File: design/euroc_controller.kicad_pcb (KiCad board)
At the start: 4 copper layers, 35.1 x 75.7 mm, 82 parts, among them J1 xt30, J2 jst_sh 4, J4 jst_sh 4, J5 jst_sh 4, J6 SMA, J7 Screw_Terminal_01x06, J8 USB_C_Receptacle_USB2.0, J9 jst_sh 4, Q1 MMBT3904, U1 TPSM5601R5, U10 VN7050ASTR, U11 VN7050ASTR, U12 STM32L562CETx, U2 USBLC6-2SC6, U3 LSM6DSO32, U4 MS5611-01BA, U5 SN65HVD232, U6 W25Q128JVS, U7 RFM69W, U8 L86, U9 VN7050ASTR, Y1 48MHz

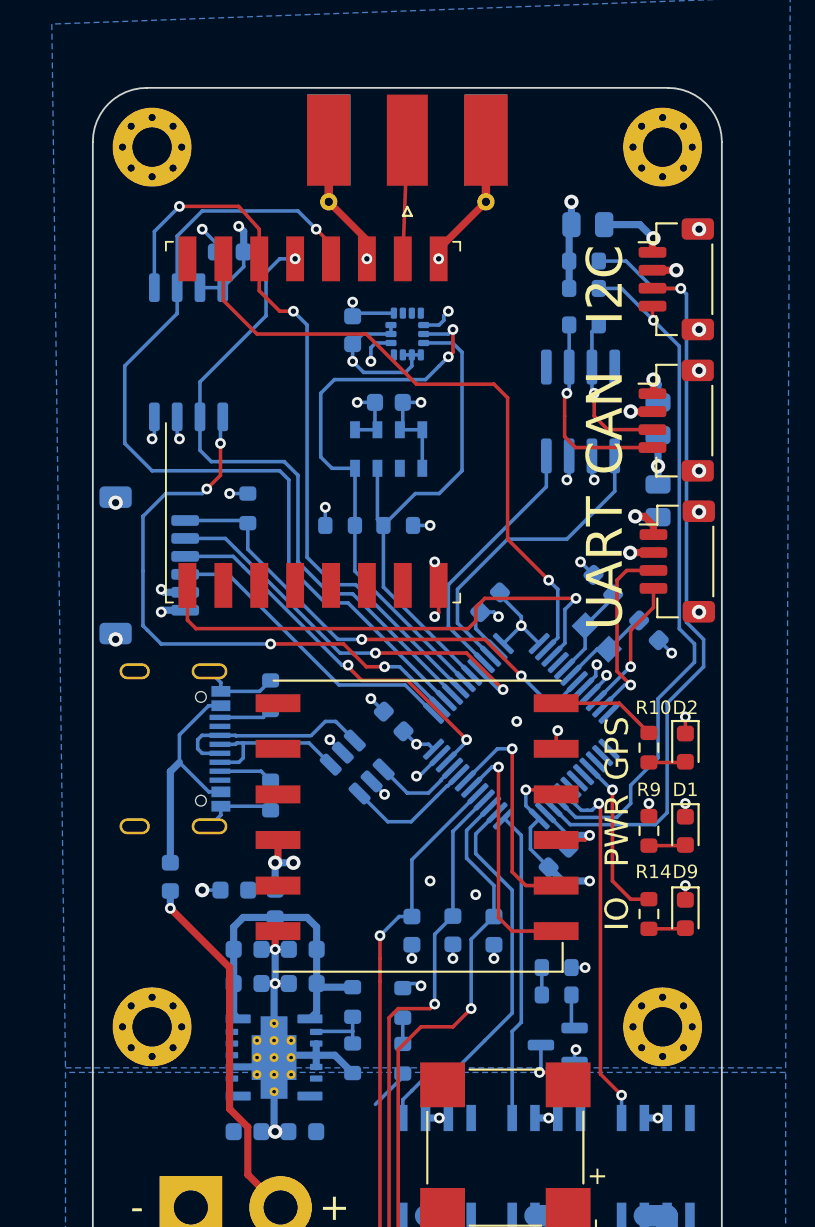
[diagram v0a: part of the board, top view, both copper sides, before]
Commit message: align mounting holes
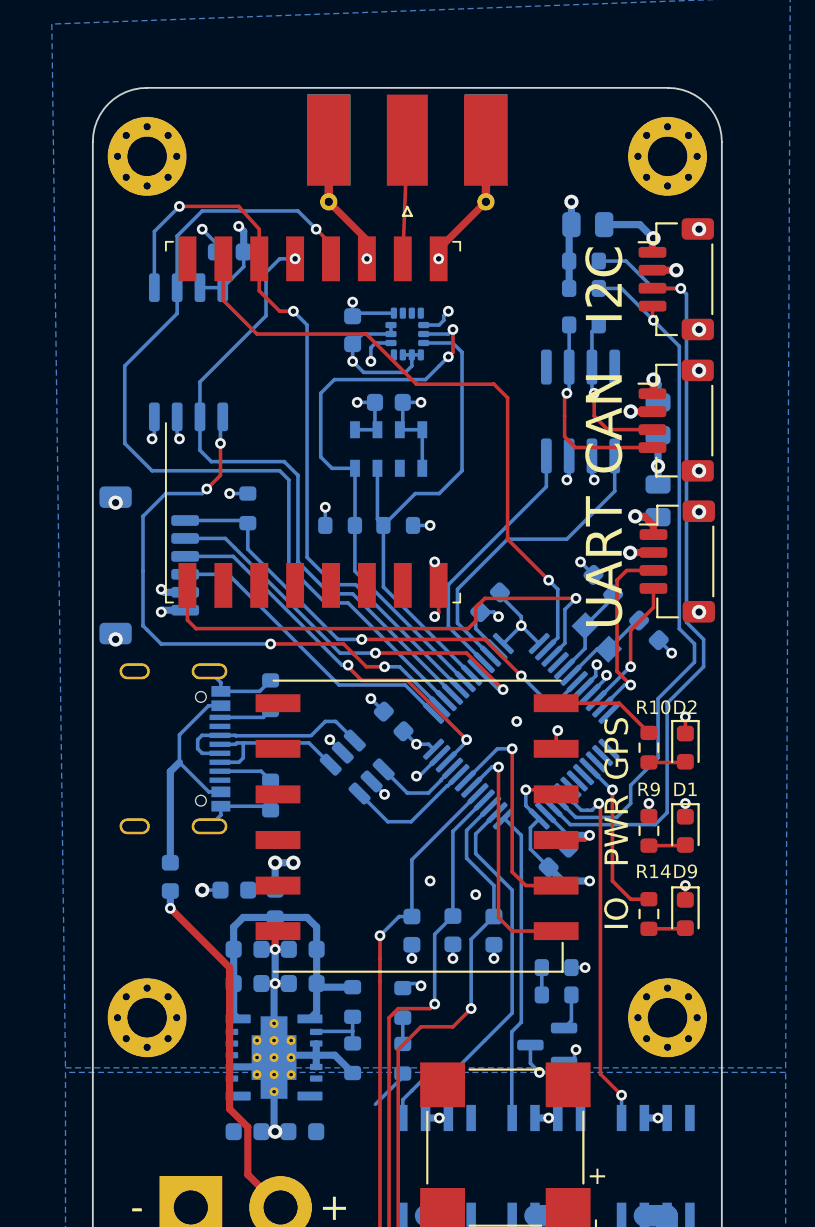
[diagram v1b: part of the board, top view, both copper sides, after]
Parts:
- removed the H1 at (196.1, 49.0)
- removed the H2 at (167.6, 49.0)
- added H3: MountingHole_Pad, MountingHole:MountingHole_2.2mm_M2_Pad_Via, F.Cu at (167.4, 97.5)
- added H4: MountingHole_Pad, MountingHole:MountingHole_2.2mm_M2_Pad_Via, F.Cu at (196.4, 97.5)
- moved H1 48.5 mm to (167.4, 49.5)
- moved H2 48.5 mm to (196.4, 49.5)
- moved Q1 0.59 mm to (189.7, 99.1)
- renumbered H3 to H1, H4 to H2
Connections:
- U8 pad 10: +3V3 -> unconnected-(U8-~{RESET}-Pad10)
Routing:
- net +3V3: track 64.1 -> 62.8 mm
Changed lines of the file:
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@@
   (net 95 "Net-(J5-Pin_1)")
   (net 96 "Net-(J4-Pin_1)")
+  (net 97 "unconnected-(U8-~{RESET}-Pad10)")
   (footprint "Connector_JST:JST_SH_BM04B-SRSS-TB_1x04-1MP_P1.00mm_Vertical" (layer "F.Cu")
     (at 196.846934 64.262 -90)
@@
       (net 42 "unconnected-(U8-NC-Pad9)") (pinfunction "NC") (pintype "no_connect"))
     (pad "10" smd rect (at 7.75 -0.77) (size 2.5 1) (layers "F.Cu" "F.Paste" "F.Mask")
-      (net 3 "+3V3") (pinfunction "~{RESET}") (pintype "input"))
+      (net 97 "unconnected-(U8-~{RESET}-Pad10)") (pinfunction "~{RESET}") (pintype "input+no_connect"))
     (pad "11" smd rect (at 7.75 -3.31) (size 2.5 1) (layers "F.Cu" "F.Paste" "F.Mask")
       (net 43 "unconnected-(U8-RESERVED-Pad11)") (pinfunction "RESERVED") (pintype "passive+no_connect"))
@@
   )
   (footprint "MountingHole:MountingHole_2.2mm_M2_Pad_Via" (layer "F.Cu")
-    (at 196.088 49.022)
+    (at 167.364 97.536)
     (descr "Mounting Hole 2.2mm, M2")
     (tags "mounting hole 2.2mm m2")
@@
     (property "ki_keywords" "mounting hole")
     (attr exclude_from_pos_files)
-    (fp_text reference "H1" (at 0 -3.2) (layer "F.SilkS") hide
+    (fp_text reference "H3" (at 0 -3.2) (layer "F.SilkS") hide
         (effects (font (size 1 1) (thickness 0.15)))
     )
@@
   )
   (footprint "MountingHole:MountingHole_2.2mm_M2_Pad_Via" (layer "F.Cu")
-    (at 167.64 49.022)
+    (at 196.364 97.536)
     (descr "Mounting Hole 2.2mm, M2")
     (tags "mounting hole 2.2mm m2")
@@
     (property "ki_keywords" "mounting hole")
     (attr exclude_from_pos_files)
-    (fp_text reference "H2" (at 0 -3.2) (layer "F.SilkS") hide
+    (fp_text reference "H4" (at 0 -3.2) (layer "F.SilkS") hide
         (effects (font (size 1 1) (thickness 0.15)))
     )
@@
   )
   (footprint "MountingHole:MountingHole_2.2mm_M2_Pad_Via" (layer "F.Cu")
-    (at 196.088 98.044)
+    (at 196.364 49.536)
     (descr "Mounting Hole 2.2mm, M2")
     (tags "mounting hole 2.2mm m2")
@@
     (property "ki_keywords" "mounting hole")
     (attr exclude_from_pos_files)
-    (fp_text reference "H4" (at 0 -3.2) (layer "F.SilkS") hide
+    (fp_text reference "H2" (at 0 -3.2) (layer "F.SilkS") hide
         (effects (font (size 1 1) (thickness 0.15)))
     )
@@
   )
   (footprint "MountingHole:MountingHole_2.2mm_M2_Pad_Via" (layer "F.Cu")
-    (at 167.64 98.044)
+    (at 167.364 49.536)
     (descr "Mounting Hole 2.2mm, M2")
     (tags "mounting hole 2.2mm m2")
@@
     (property "ki_keywords" "mounting hole")
     (attr exclude_from_pos_files)
-    (fp_text reference "H3" (at 0 -3.2) (layer "F.SilkS") hide
+    (fp_text reference "H1" (at 0 -3.2) (layer "F.SilkS") hide
         (effects (font (size 1 1) (thickness 0.15)))
     )
@@
   )
   (footprint "Package_TO_SOT_SMD:SOT-23" (layer "B.Cu")
-    (at 190.246 99.06 180)
+    (at 189.6595 99.06 180)
     (descr "SOT, 3 Pin (https://www.jedec.org/system/files/docs/to-236h.pdf variant AB), generated with kicad-footprint-generator ipc_gullwing_generator.py")
     (tags "SOT TO_SOT_SMD")
@@
     (property "ki_keywords" "NPN Transistor")
     (attr smd)
-    (fp_text reference "Q1" (at 1.778 1.27) (layer "B.SilkS")
+    (fp_text reference "Q1" (at 1.9535 1.27) (layer "B.SilkS")
         (effects (font (size 1 1) (thickness 0.15)) (justify mirror))
     )
@@
   (segment (start 174.437 95.692) (end 174.498 95.631) (width 0.4) (layer "B.Cu") (net 1))
   (segment (start 190.834016 87.376004) (end 189.566342 86.10833) (width 0.2) (layer "B.Cu") (net 1))
-  (segment (start 191.1835 100.01) (end 191.1835 99.3925) (width 0.2) (layer "B.Cu") (net 1))
   (segment (start 191.389 116.002) (end 190.551 116.84) (width 0.8) (layer "B.Cu") (net 1))
   (segment (start 165.608 68.82) (end 165.608 68.834) (width 0.4) (layer "B.Cu") (net 1))
@@
   (segment (start 191.389 114.808) (end 191.389 116.002) (width 0.8) (layer "B.Cu") (net 1))
   (segment (start 191.1835 99.3925) (end 191.262 99.314) (width 0.2) (layer "B.Cu") (net 1))
+  (segment (start 191.1835 99.822) (end 191.1835 99.3925) (width 0.2) (layer "B.Cu") (net 1))
   (segment (start 184.404 93.4465) (end 184.404 94.234) (width 0.2) (layer "B.Cu") (net 1))
   (segment (start 186.69 74.93) (end 186.944 75.184) (width 0.2) (layer "B.Cu") (net 1))
@@
   (segment (start 179.874334 84.370334) (end 180.594 85.09) (width 0.2) (layer "B.Cu") (net 1))
   (segment (start 182.532028 84.074) (end 182.372 84.074) (width 0.2) (layer "B.Cu") (net 1))
+  (segment (start 190.9955 100.01) (end 191.1835 99.822) (width 0.2) (layer "B.Cu") (net 1))
   (segment (start 171.471 86.239) (end 170.84 86.87) (width 0.2) (layer "B.Cu") (net 1))
   (segment (start 169.48151 73.82764) (end 168.31564 73.82764) (width 0.4) (layer "B.Cu") (net 1))
@@
   (segment (start 195.874008 76.494008) (end 196.596 77.216) (width 0.2) (layer "B.Cu") (net 1))
   (segment (start 165.608 76.42) (end 165.608 76.454) (width 0.4) (layer "B.Cu") (net 1))
+  (segment (start 190.597 100.01) (end 190.9955 100.01) (width 0.2) (layer "B.Cu") (net 1))
   (segment (start 182.114 61.218) (end 181.756 61.576) (width 0.2) (layer "B.Cu") (net 1))
   (segment (start 173.634 79.35) (end 174.244 78.74) (width 0.2) (layer "B.Cu") (net 1))
@@
   (segment (start 189.903945 84.836) (end 190.157945 85.09) (width 0.2) (layer "F.Cu") (net 3))
   (segment (start 191.77 110.744) (end 192.532 110.744) (width 0.4) (layer "F.Cu") (net 3))
-  (segment (start 174.657945 88.740055) (end 174.498 88.9) (width 0.4) (layer "F.Cu") (net 3))
   (segment (start 183.61 72.358) (end 183.388 72.136) (width 0.2) (layer "F.Cu") (net 3))
   (segment (start 183.61 73.445) (end 183.61 74.962) (width 0.2) (layer "F.Cu") (net 3))
   (segment (start 183.61 73.445) (end 183.61 72.358) (width 0.2) (layer "F.Cu") (net 3))
-  (segment (start 174.657945 87.63) (end 174.657945 88.740055) (width 0.4) (layer "F.Cu") (net 3))
   (segment (start 190.825 109.799) (end 191.77 110.744) (width 0.4) (layer "F.Cu") (net 3))
   (segment (start 195.326 86.297) (end 195.326 85.598) (width 0.2) (layer "F.Cu") (net 3))
@@
   (segment (start 190.134 100.584) (end 190.825 101.275) (width 0.2) (layer "F.Cu") (net 4))
   (via (at 189.23 100.584) (size 0.6) (drill 0.3) (layers "F.Cu" "B.Cu") (net 4))
-  (segment (start 189.3085 99.06) (end 189.3085 100.5055) (width 0.2) (layer "B.Cu") (net 4))
-  (segment (start 189.3085 100.5055) (end 189.23 100.584) (width 0.2) (layer "B.Cu") (net 4))
+  (segment (start 188.722 99.06) (end 188.722 100.076) (width 0.2) (layer "B.Cu") (net 4))
+  (segment (start 188.722 100.076) (end 189.23 100.584) (width 0.2) (layer "B.Cu") (net 4))
   (segment (start 197.3205 87.947) (end 197.358 87.9095) (width 0.2) (layer "F.Cu") (net 5))
   (segment (start 195.326 87.947) (end 197.3205 87.947) (width 0.2) (layer "F.Cu") (net 5))
@@
   (segment (start 192.154 85.976) (end 192.532 85.598) (width 0.2) (layer "B.Cu") (net 82))
   (segment (start 191.894 85.976) (end 192.154 85.976) (width 0.2) (layer "B.Cu") (net 82))
+  (segment (start 187.706 103.124) (end 187.6845 103.1025) (width 0.2) (layer "B.Cu") (net 83))
   (segment (start 187.299884 86.461884) (end 188.214 87.376) (width 0.2) (layer "B.Cu") (net 83))
-  (segment (start 187.706 98.298) (end 187.706 103.124) (width 0.2) (layer "B.Cu") (net 83))
-  (segment (start 188.214 97.79) (end 187.706 98.298) (width 0.2) (layer "B.Cu") (net 83))
+  (segment (start 187.6845 98.3195) (end 188.214 97.79) (width 0.2) (layer "B.Cu") (net 83))
   (segment (start 187.215212 86.461884) (end 187.299884 86.461884) (width 0.2) (layer "B.Cu") (net 83))
+  (segment (start 187.6845 103.1025) (end 187.6845 98.3195) (width 0.2) (layer "B.Cu") (net 83))
   (segment (start 188.214 87.376) (end 188.214 97.79) (width 0.2) (layer "B.Cu") (net 83))
   (segment (start 181.61 103.124) (end 181.61 102.108) (width 0.2) (layer "B.Cu") (net 84))
@@
   (segment (start 186.948652 79.248) (end 187.198 79.248) (width 0.2) (layer "B.Cu") (net 90))
   (segment (start 185.800998 78.100346) (end 186.948652 79.248) (width 0.2) (layer "B.Cu") (net 90))
+  (segment (start 191.008 97.699) (end 190.597 98.11) (width 0.2) (layer "B.Cu") (net 91))
   (segment (start 191.008 97.9345) (end 191.1835 98.11) (width 0.2) (layer "B.Cu") (net 91))
-  (segment (start 191.008 96.266) (end 191.008 97.9345) (width 0.2) (layer "B.Cu") (net 91))
+  (segment (start 191.008 96.266) (end 191.008 97.699) (width 0.2) (layer "B.Cu") (net 91))
   (segment (start 170.434 82.804) (end 170.438 82.8) (width 0.2) (layer "B.Cu") (net 92))
   (segment (start 171.42 81.8) (end 172.290001 81.8) (width 0.2) (layer "B.Cu") (net 92))

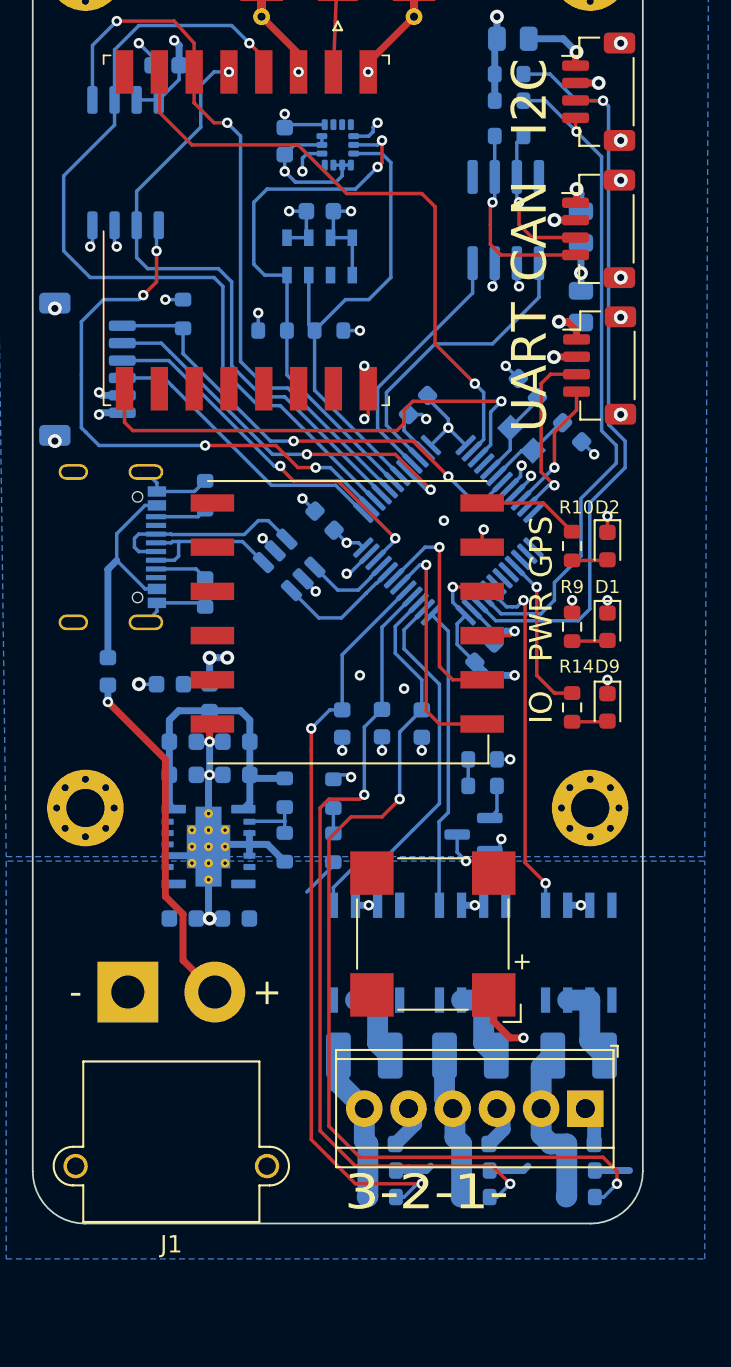
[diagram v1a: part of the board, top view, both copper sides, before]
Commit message: use real clock, fix esd vbus
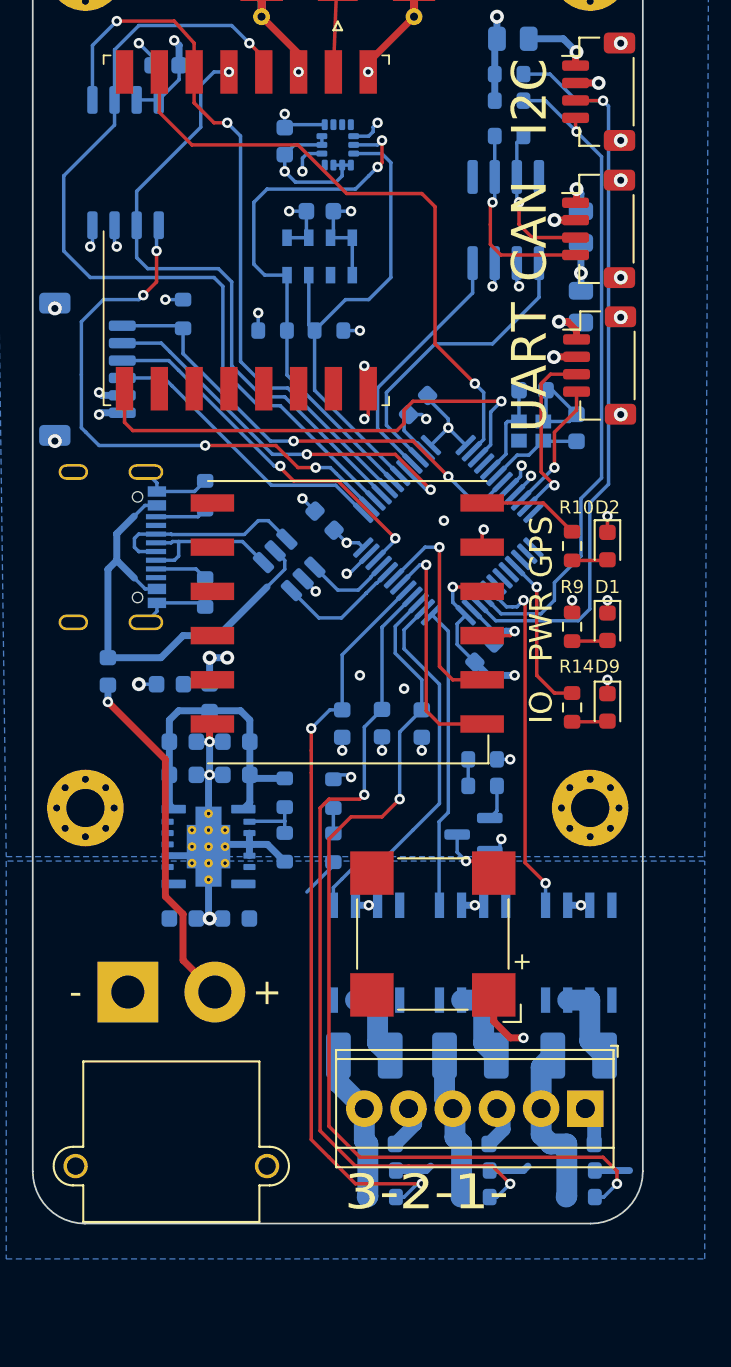
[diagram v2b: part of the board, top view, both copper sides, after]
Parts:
- Y1: footprint Crystal:Crystal_SMD_2012-2Pin_2.0x1.2mm_HandSoldering -> Crystal:Crystal_SMD_2016-4Pin_2.0x1.6mm
- moved Y1 0.72 mm to (193.0, 75.9), turned to 0 degrees
- moved C14 0.36 mm to (195.6, 75.7), turned to 90 degrees
- moved C13 0.30 mm to (193.1, 73.5), turned to 0 degrees
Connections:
- D10 pad 2: Net-(D10-A) -> /VBUS
- J8 pad A4: Net-(D10-A) -> /VBUS
- J8 pad A9: Net-(D10-A) -> /VBUS
- J8 pad B4: Net-(D10-A) -> /VBUS
- J8 pad B9: Net-(D10-A) -> /VBUS
- U2 pad 5: +3V3 -> /VBUS
- Y1 pad 2: /OSC_OUT -> Earth
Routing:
- net /VBUS: track 0.00 -> 26.9 mm
- net Net-(D10-A): track 13.3 -> 0.00 mm
- net Earth: track 98.0 -> 102.3 mm, vias 46 -> 44
- net +3V3: track 62.8 -> 61.8 mm, vias 26 -> 25
- net /EXT_SDA: track 44.5 -> 43.7 mm
- net /EXT_SCL: track 38.7 -> 38.0 mm

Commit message: update ioc, add logo
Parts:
- added G***: LOGO, lib:aesir_short, F.Cu at (174.2, 100.8)
- added G***: LOGO, lib:euroc, F.Cu at (169.2, 90.4)
- added G***: LOGO, lib:euroc, F.Cu at (195.8, 105.2)
- added G***: LOGO, lib:euroc, B.Cu at (172.5, 114.6)
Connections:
- U12 pad 13: unconnected-(U12-PA3-Pad13) -> /BUZZER
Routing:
- net /BUZZER: track 1.52 -> 20.0 mm, vias 0 -> 2
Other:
- board text added: "Fjalar V1.0 May 2023"
- board text removed: "Align mounting holes"

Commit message: oof new umc (st32u5)
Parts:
- removed U12: STM32L562CETx, Package_QFP:LQFP-48_7x7mm_P0.5mm
- added U13: STM32U575CGTx, Package_QFP:LQFP-48_7x7mm_P0.5mm, B.Cu at (188.2, 81.6)
- C12: value 100p -> 4u7
- moved C12 0.95 mm to (191.2, 88.4)
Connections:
- C12 pad 1: +3V3 -> Earth
- C12 pad 2: Earth -> Net-(U13-VCAP)
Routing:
- net /PYRO3_SENSE: track 54.4 -> 76.6 mm, vias 2 -> 4
- net +3V3: track 61.8 -> 55.8 mm, vias 25 -> 24
- net Net-(U13-VCAP): track 0.00 -> 2.90 mm
- net /PYRO1_EN: track 21.6 -> 19.2 mm
- net /PYRO2_EN: track 17.4 -> 19.7 mm
- net /EXT_SDA: track 43.7 -> 42.4 mm
- net /PYRO3_EN: track 20.5 -> 19.8 mm
- net /EXT_SCL: track 38.0 -> 38.7 mm, vias 1 -> 2
- net Earth: track 102.3 -> 101.9 mm, vias 44 -> 43
